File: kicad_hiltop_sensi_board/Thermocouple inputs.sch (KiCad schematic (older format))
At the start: 52 parts, among them U23 MAX4194

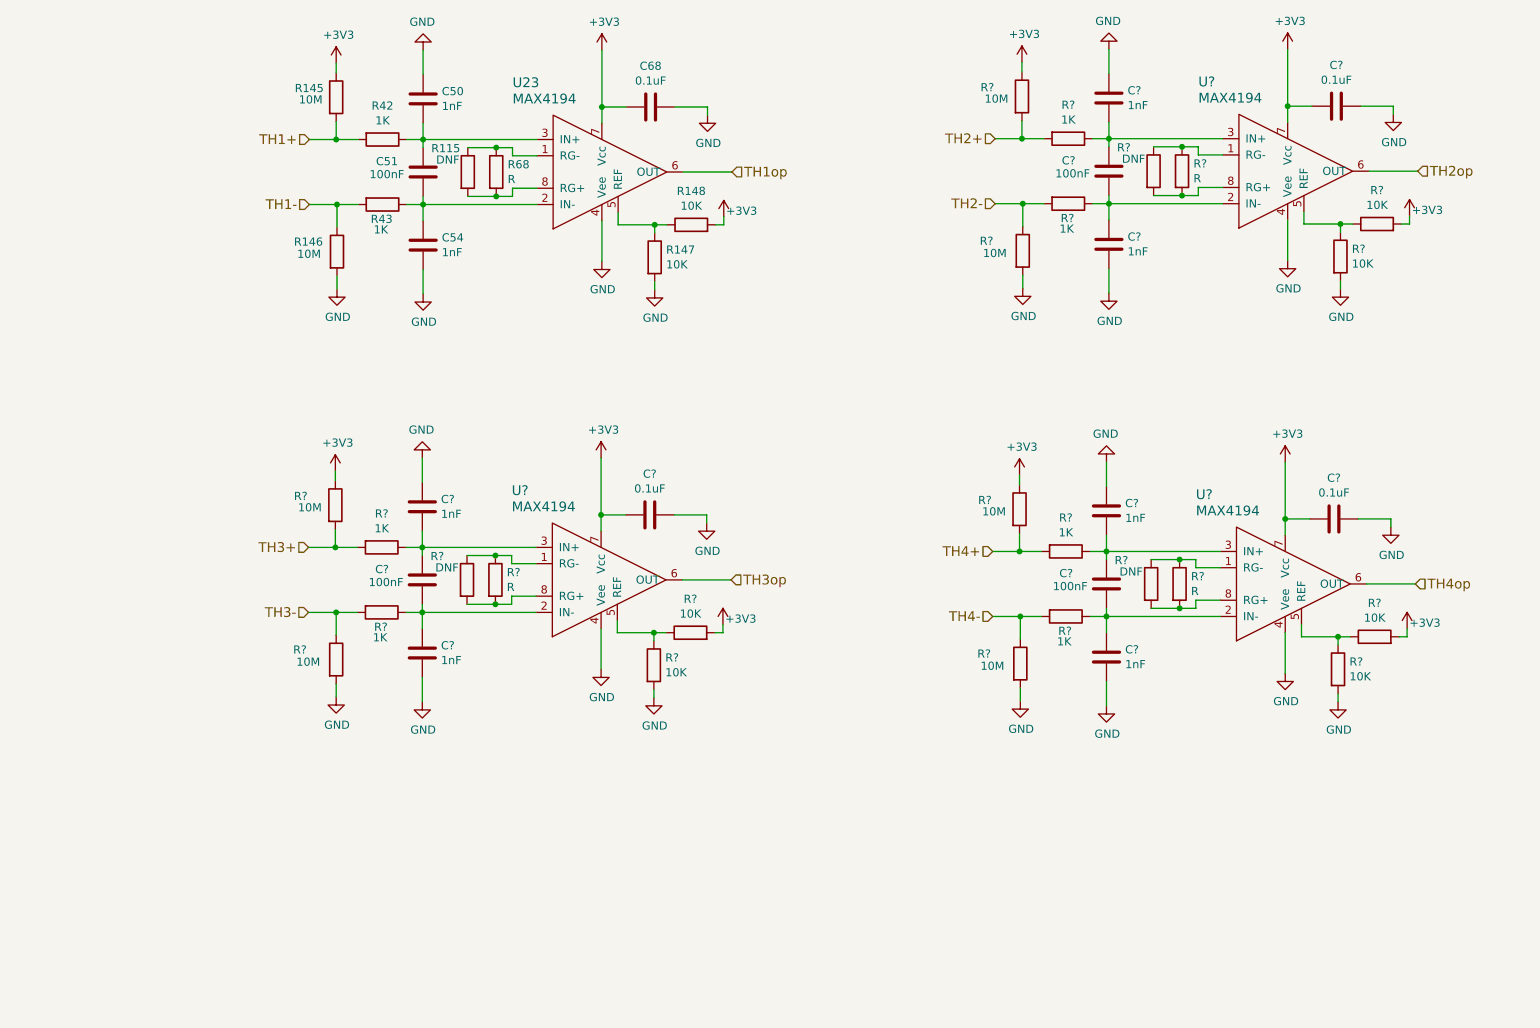
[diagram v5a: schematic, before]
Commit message: Sensi board schematic updated from comments
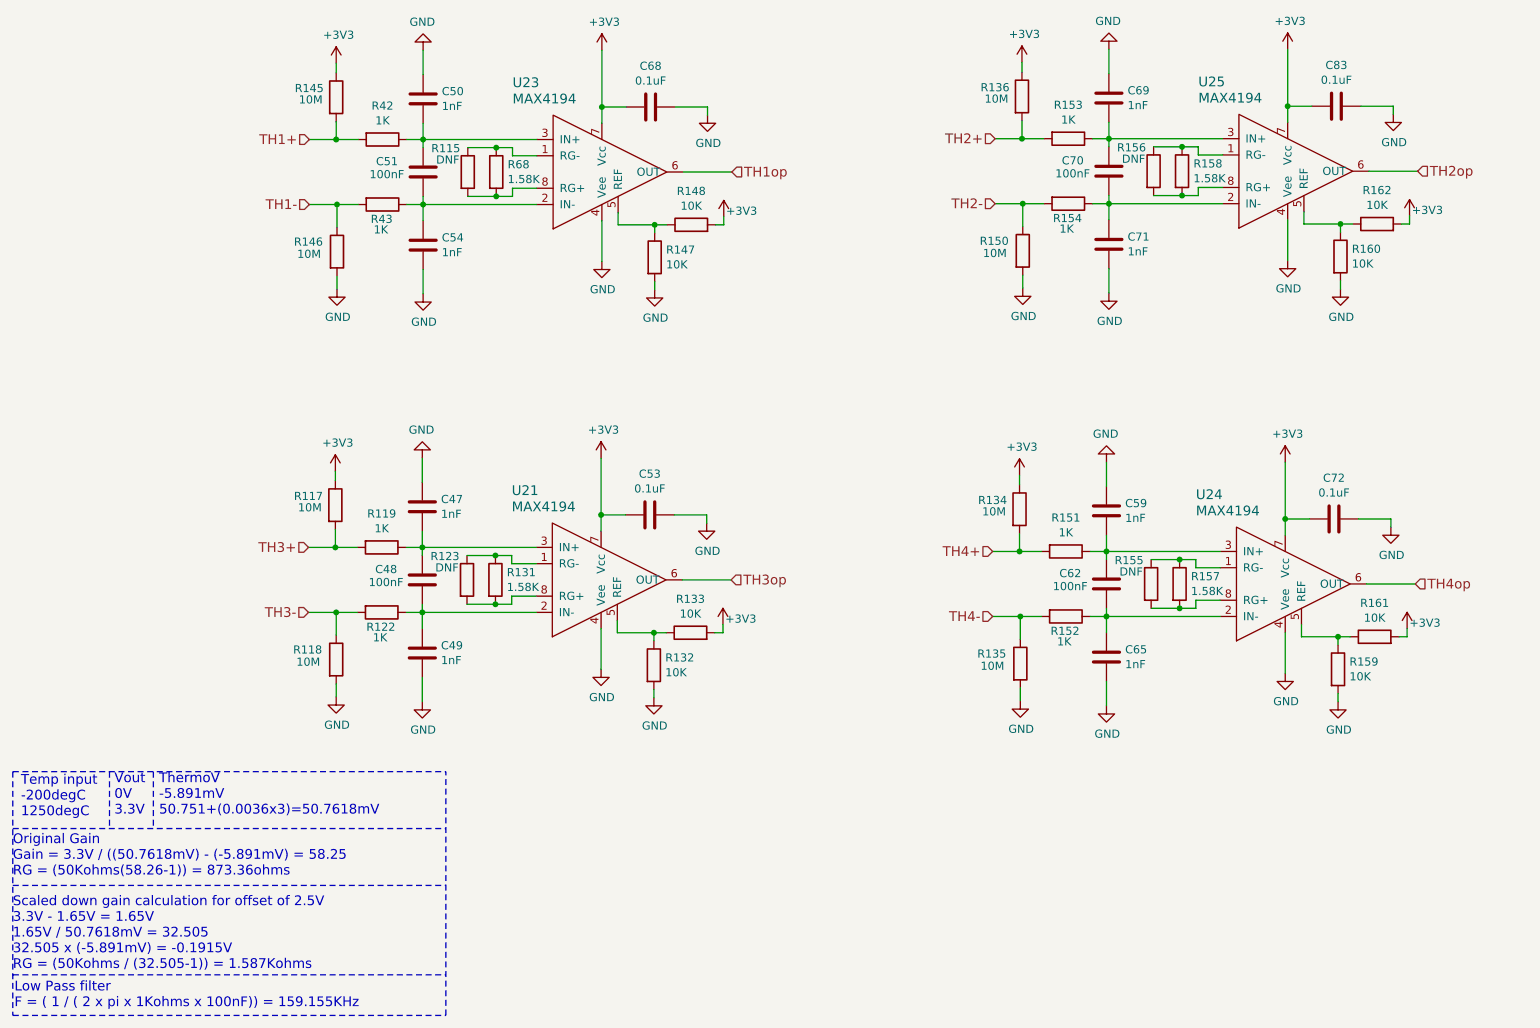
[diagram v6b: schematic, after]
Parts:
- R131, R157, R158: renamed from R?; value R -> 1.58K; Devtank (none) -> 103-005
- R68: value R -> 1.58K; Devtank (none) -> 103-005
- gave numbers to parts that had none: 36
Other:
- note added: "Low Pass filter\nF = ( 1 / ( 2 x pi x 1Kohms x 100nF)) = 159.155KHz"
- note added: "Original Gain\nGain = 3.3V / ((50.7618mV) - (-5.891mV) = 58.25\nRG = (50Kohms(58.26-1)) = 873.36ohms"
- note added: "Scaled down gain calculation for offset of 2.5V\n3.3V - 1.65V = 1.65V\n1.65V / 50.7618mV = 32.505\n32.505 x (-5.891mV) = -0.1915V\nRG = (50Kohms / (32.505-1)) = 1.587Kohms\n"
- note added: "Temp input \n-200degC\n1250degC"
- note added: "ThermoV\n-5.891mV\n50.751+(0.0036x3)=50.7618mV"
- note added: "Vout\n0V\n3.3V\n"

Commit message: Updated sensi board layout
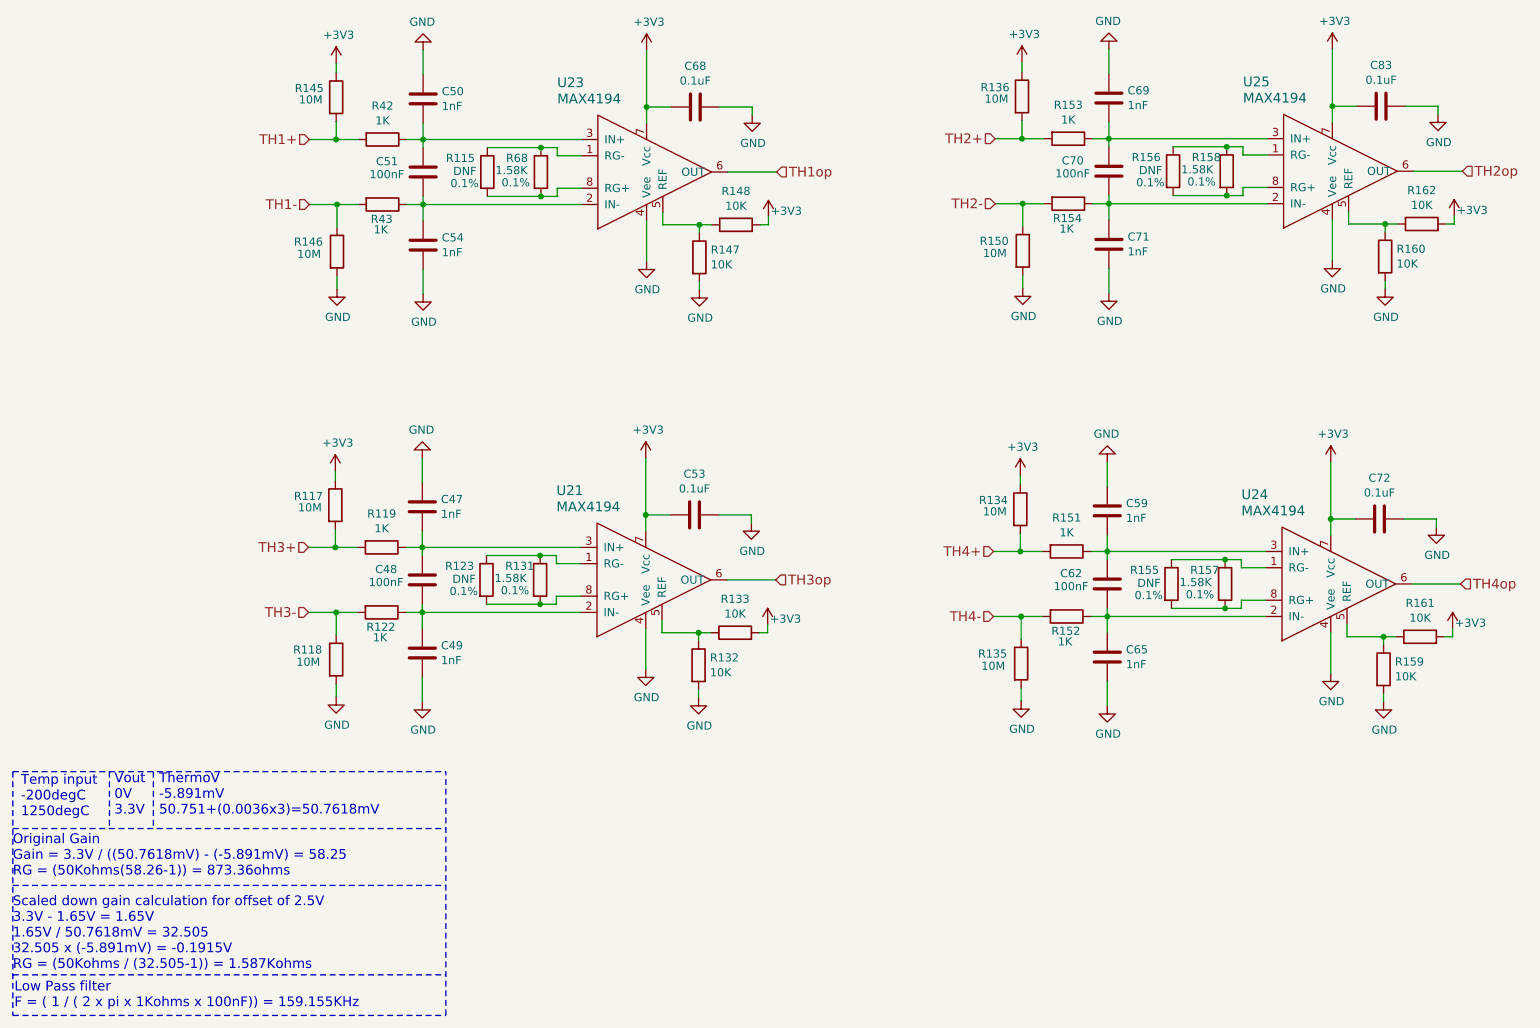
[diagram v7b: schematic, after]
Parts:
- R115, R123, R155, R156: Tolerance (none) -> 0.1%
- R117, R118, R132, R133, R134, R135, R136, R145, R146, R147, R148, R150, R159, R160, R161, R162: footprint (none) -> Resistor_SMD:R_0603_1608Metric
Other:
- moved on the sheet: C68, R115, R147, R148, R68, U23

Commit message: Sensi Board Complete
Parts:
- C47, C49, C50, C54, C59, C65, C69, C71: Devtank (none) -> 106-004
- C48, C51, C62, C70: Devtank (none) -> 105-002
- R117, R118, R134, R135, R136, R145, R146, R150: Devtank (none) -> 101-057
- R119, R122, R151, R152, R153, R154, R42, R43: Devtank (none) -> 101-012
- R132, R133, R147, R148, R159, R160, R161, R162: Devtank (none) -> 101-010
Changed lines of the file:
@@
 F 2 "Capacitor_SMD:C_0603_1608Metric" H 3438 2500 50  0001 C CNN
 F 3 "" H 3400 2650 50  0001 C CNN
+F 4 "106-004" H 3400 2650 50  0001 C CNN "Devtank"
 	1    3400 2650
 	1    0    0    -1
@@
 F 2 "Capacitor_SMD:C_0603_1608Metric" H 3438 1600 50  0001 C CNN
 F 3 "" H 3400 1750 50  0001 C CNN
+F 4 "106-004" H 3400 1750 50  0001 C CNN "Devtank"
 	1    3400 1750
 	1    0    0    -1
@@
 F 2 "Capacitor_SMD:C_0603_1608Metric" H 3438 2050 50  0001 C CNN
 F 3 "" H 3400 2200 50  0001 C CNN
+F 4 "105-002" H 3400 2200 50  0001 C CNN "Devtank"
 	1    3400 2200
 	1    0    0    -1
@@
 F 2 "Resistor_SMD:R_0603_1608Metric" V 3080 2000 50  0001 C CNN
 F 3 "" H 3150 2000 50  0001 C CNN
+F 4 "101-012" H 3150 2000 50  0001 C CNN "Devtank"
 	1    3150 2000
 	0    1    1    0
@@
 F 2 "Resistor_SMD:R_0603_1608Metric" V 3080 2400 50  0001 C CNN
 F 3 "" H 3150 2400 50  0001 C CNN
+F 4 "101-012" H 3150 2400 50  0001 C CNN "Devtank"
 	1    3150 2400
 	0    1    1    0
@@
 F 2 "Resistor_SMD:R_0603_1608Metric" V 2800 2690 50  0001 C CNN
 F 3 "" H 2870 2690 50  0001 C CNN
+F 4 "101-057" H 2870 2690 50  0001 C CNN "Devtank"
 	1    2870 2690
 	1    0    0    -1
@@
 F 2 "Resistor_SMD:R_0603_1608Metric" V 2795 1740 50  0001 C CNN
 F 3 "" H 2865 1740 50  0001 C CNN
+F 4 "101-057" H 2865 1740 50  0001 C CNN "Devtank"
 	1    2865 1740
 	1    0    0    -1
@@
 F 2 "Resistor_SMD:R_0603_1608Metric" V 5255 2525 50  0001 C CNN
 F 3 "" H 5325 2525 50  0001 C CNN
+F 4 "101-010" H 5325 2525 50  0001 C CNN "Devtank"
 	1    5325 2525
 	0    -1   -1   0
@@
 F 2 "Resistor_SMD:R_0603_1608Metric" V 5030 2725 50  0001 C CNN
 F 3 "" H 5100 2725 50  0001 C CNN
+F 4 "101-010" H 5100 2725 50  0001 C CNN "Devtank"
 	1    5100 2725
 	1    0    0    -1
@@
 F 2 "Capacitor_SMD:C_0603_1608Metric" H 7658 2495 50  0001 C CNN
 F 3 "" H 7620 2645 50  0001 C CNN
+F 4 "106-004" H 7620 2645 50  0001 C CNN "Devtank"
 	1    7620 2645
 	1    0    0    -1
@@
 F 2 "Capacitor_SMD:C_0603_1608Metric" H 7658 1595 50  0001 C CNN
 F 3 "" H 7620 1745 50  0001 C CNN
+F 4 "106-004" H 7620 1745 50  0001 C CNN "Devtank"
 	1    7620 1745
 	1    0    0    -1
@@
 F 2 "Capacitor_SMD:C_0603_1608Metric" H 7658 2045 50  0001 C CNN
 F 3 "" H 7620 2195 50  0001 C CNN
+F 4 "105-002" H 7620 2195 50  0001 C CNN "Devtank"
 	1    7620 2195
 	1    0    0    -1
@@
 F 2 "Resistor_SMD:R_0603_1608Metric" V 7300 1995 50  0001 C CNN
 F 3 "" H 7370 1995 50  0001 C CNN
+F 4 "101-012" H 7370 1995 50  0001 C CNN "Devtank"
 	1    7370 1995
 	0    1    1    0
@@
 F 2 "Resistor_SMD:R_0603_1608Metric" V 7300 2395 50  0001 C CNN
 F 3 "" H 7370 2395 50  0001 C CNN
+F 4 "101-012" H 7370 2395 50  0001 C CNN "Devtank"
 	1    7370 2395
 	0    1    1    0
@@
 F 2 "Resistor_SMD:R_0603_1608Metric" V 7020 2685 50  0001 C CNN
 F 3 "" H 7090 2685 50  0001 C CNN
+F 4 "101-057" H 7090 2685 50  0001 C CNN "Devtank"
 	1    7090 2685
 	1    0    0    -1
@@
 F 2 "Resistor_SMD:R_0603_1608Metric" V 7015 1735 50  0001 C CNN
 F 3 "" H 7085 1735 50  0001 C CNN
+F 4 "101-057" H 7085 1735 50  0001 C CNN "Devtank"
 	1    7085 1735
 	1    0    0    -1
@@
 F 2 "Resistor_SMD:R_0603_1608Metric" V 9475 2520 50  0001 C CNN
 F 3 "" H 9545 2520 50  0001 C CNN
+F 4 "101-010" H 9545 2520 50  0001 C CNN "Devtank"
 	1    9545 2520
 	0    -1   -1   0
@@
 F 2 "Resistor_SMD:R_0603_1608Metric" V 9250 2720 50  0001 C CNN
 F 3 "" H 9320 2720 50  0001 C CNN
+F 4 "101-010" H 9320 2720 50  0001 C CNN "Devtank"
 	1    9320 2720
 	1    0    0    -1
@@
 F 2 "Capacitor_SMD:C_0603_1608Metric" H 3433 5010 50  0001 C CNN
 F 3 "" H 3395 5160 50  0001 C CNN
+F 4 "106-004" H 3395 5160 50  0001 C CNN "Devtank"
 	1    3395 5160
 	1    0    0    -1
@@
 F 2 "Capacitor_SMD:C_0603_1608Metric" H 3433 4110 50  0001 C CNN
 F 3 "" H 3395 4260 50  0001 C CNN
+F 4 "106-004" H 3395 4260 50  0001 C CNN "Devtank"
 	1    3395 4260
 	1    0    0    -1
@@
 F 2 "Capacitor_SMD:C_0603_1608Metric" H 3433 4560 50  0001 C CNN
 F 3 "" H 3395 4710 50  0001 C CNN
+F 4 "105-002" H 3395 4710 50  0001 C CNN "Devtank"
 	1    3395 4710
 	1    0    0    -1
@@
 F 2 "Resistor_SMD:R_0603_1608Metric" V 3075 4510 50  0001 C CNN
 F 3 "" H 3145 4510 50  0001 C CNN
+F 4 "101-012" H 3145 4510 50  0001 C CNN "Devtank"
 	1    3145 4510
 	0    1    1    0
@@
 F 2 "Resistor_SMD:R_0603_1608Metric" V 3075 4910 50  0001 C CNN
 F 3 "" H 3145 4910 50  0001 C CNN
+F 4 "101-012" H 3145 4910 50  0001 C CNN "Devtank"
 	1    3145 4910
 	0    1    1    0
@@
 F 2 "Resistor_SMD:R_0603_1608Metric" V 2795 5200 50  0001 C CNN
 F 3 "" H 2865 5200 50  0001 C CNN
+F 4 "101-057" H 2865 5200 50  0001 C CNN "Devtank"
 	1    2865 5200
 	1    0    0    -1
@@
 F 2 "Resistor_SMD:R_0603_1608Metric" V 2790 4250 50  0001 C CNN
 F 3 "" H 2860 4250 50  0001 C CNN
+F 4 "101-057" H 2860 4250 50  0001 C CNN "Devtank"
 	1    2860 4250
 	1    0    0    -1
@@
 F 2 "Resistor_SMD:R_0603_1608Metric" V 5250 5035 50  0001 C CNN
 F 3 "" H 5320 5035 50  0001 C CNN
+F 4 "101-010" H 5320 5035 50  0001 C CNN "Devtank"
 	1    5320 5035
 	0    -1   -1   0
@@
 F 2 "Resistor_SMD:R_0603_1608Metric" V 5025 5235 50  0001 C CNN
 F 3 "" H 5095 5235 50  0001 C CNN
+F 4 "101-010" H 5095 5235 50  0001 C CNN "Devtank"
 	1    5095 5235
 	1    0    0    -1
@@
 F 2 "Capacitor_SMD:C_0603_1608Metric" H 7648 5035 50  0001 C CNN
 F 3 "" H 7610 5185 50  0001 C CNN
+F 4 "106-004" H 7610 5185 50  0001 C CNN "Devtank"
 	1    7610 5185
 	1    0    0    -1
@@
 F 2 "Capacitor_SMD:C_0603_1608Metric" H 7648 4135 50  0001 C CNN
 F 3 "" H 7610 4285 50  0001 C CNN
+F 4 "106-004" H 7610 4285 50  0001 C CNN "Devtank"
 	1    7610 4285
 	1    0    0    -1
@@
 F 2 "Capacitor_SMD:C_0603_1608Metric" H 7648 4585 50  0001 C CNN
 F 3 "" H 7610 4735 50  0001 C CNN
+F 4 "105-002" H 7610 4735 50  0001 C CNN "Devtank"
 	1    7610 4735
 	1    0    0    -1
@@
 F 2 "Resistor_SMD:R_0603_1608Metric" V 7290 4535 50  0001 C CNN
 F 3 "" H 7360 4535 50  0001 C CNN
+F 4 "101-012" H 7360 4535 50  0001 C CNN "Devtank"
 	1    7360 4535
 	0    1    1    0
@@
 F 2 "Resistor_SMD:R_0603_1608Metric" V 7290 4935 50  0001 C CNN
 F 3 "" H 7360 4935 50  0001 C CNN
+F 4 "101-012" H 7360 4935 50  0001 C CNN "Devtank"
 	1    7360 4935
 	0    1    1    0
@@
 F 2 "Resistor_SMD:R_0603_1608Metric" V 7010 5225 50  0001 C CNN
 F 3 "" H 7080 5225 50  0001 C CNN
+F 4 "101-057" H 7080 5225 50  0001 C CNN "Devtank"
 	1    7080 5225
 	1    0    0    -1
@@
 F 2 "Resistor_SMD:R_0603_1608Metric" V 7005 4275 50  0001 C CNN
 F 3 "" H 7075 4275 50  0001 C CNN
+F 4 "101-057" H 7075 4275 50  0001 C CNN "Devtank"
 	1    7075 4275
 	1    0    0    -1
@@
 F 2 "Resistor_SMD:R_0603_1608Metric" V 9465 5060 50  0001 C CNN
 F 3 "" H 9535 5060 50  0001 C CNN
+F 4 "101-010" H 9535 5060 50  0001 C CNN "Devtank"
 	1    9535 5060
 	0    -1   -1   0
@@
 F 2 "Resistor_SMD:R_0603_1608Metric" V 9240 5260 50  0001 C CNN
 F 3 "" H 9310 5260 50  0001 C CNN
+F 4 "101-010" H 9310 5260 50  0001 C CNN "Devtank"
 	1    9310 5260
 	1    0    0    -1
